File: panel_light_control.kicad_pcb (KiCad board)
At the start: 4 copper layers, 90 x 100 mm, 150 parts, among them J1 Conn_01x02, J11 RJ45_Shielded, J13 HR911105A, J2 RJ45_Shielded, J6 Conn_01x04, Q1 IRF540N, Q2 IRF540N, Q3 IRF540N, U1 L7805, U2 LM324, U3 STM32F207VGT6, U4 MCP2562-E-P, U5 LAN8720A, Y1 Crystal_GND24

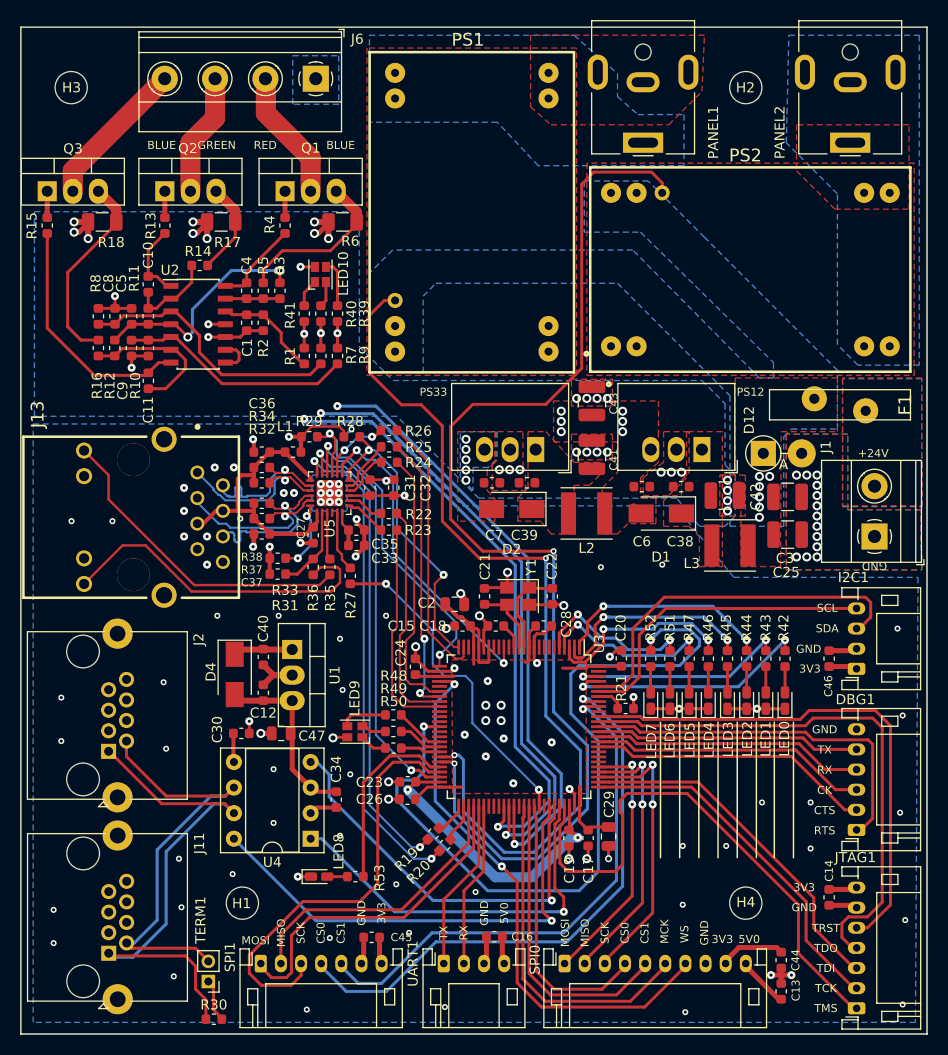
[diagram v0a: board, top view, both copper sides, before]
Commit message: Changes to 3.3V polygon shape to remove overlap with 24V, 12V input section. Some improvements and corrections to the silkscreen. 7805 location checked for 78B05 clearance - will work in case 5V >100 mA is needed :)
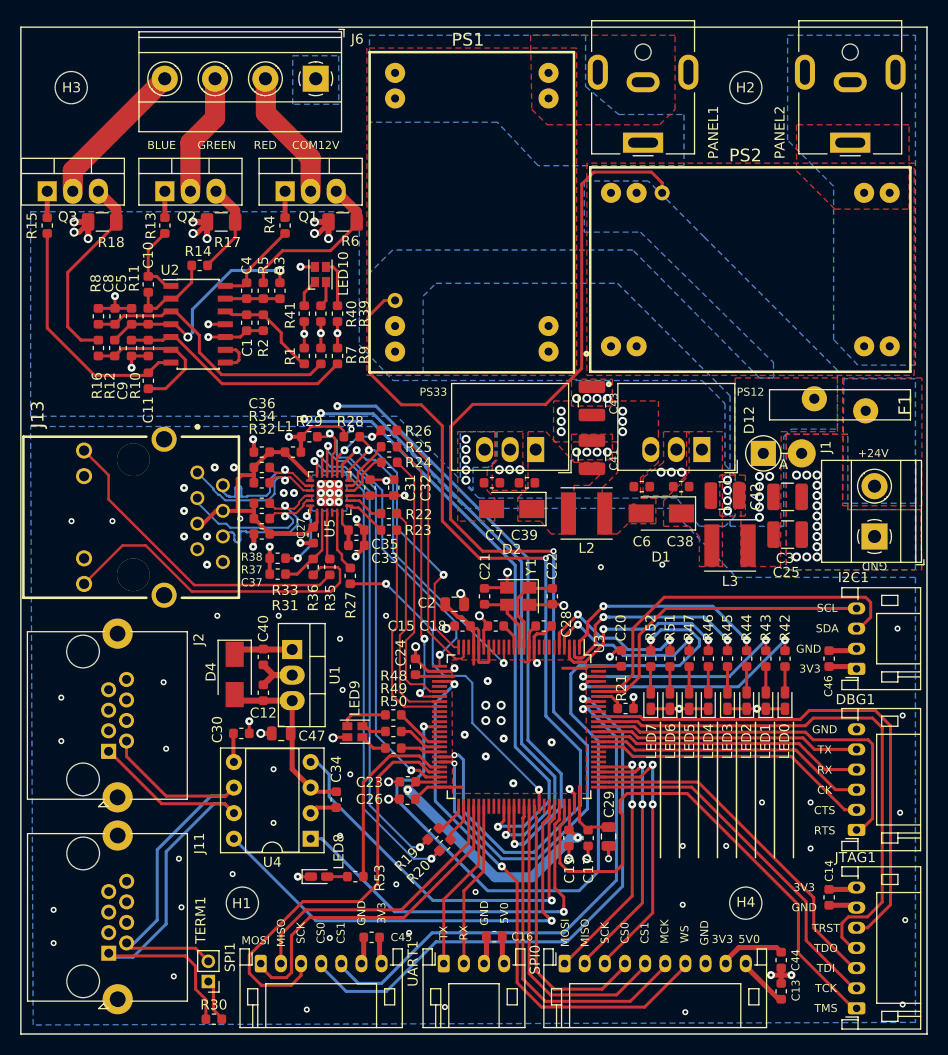
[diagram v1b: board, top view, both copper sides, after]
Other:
- board text added: "(+)"
- board text added: "+12VCOM"
- board text added: "1ACT"
- board text added: "2SPD"
- board text added: "CAN"
- board text added: "CANH"
- board text added: "CANL"
- board text added: "CAN_THRU"
- board text added: "COM12V"
- board text added: "DBG1"
- board text added: "I2C1"
- board text added: "JTAG1"
- board text added: "K_BLUE"
- board text added: "K_GREEN"
- board text added: "K_RED"
- board text added: "PANEL1"
- board text added: "PANEL2"
- board text added: "PWR IN"
- board text added: "RGB LED OUT"
- board text added: "RXN"
- board text added: "RXP"
- board text added: "SPI0/I2S"
- board text added: "SPI1"
- board text added: "TXN"
- board text added: "TXP"
- board text added: "UART1"
- board text removed: "+12V"
- board text removed: "BLUE-K"
- board text removed: "CAN1"
- board text removed: "CAN2"
- board text removed: "GREEN-K"
- board text removed: "RED-K"

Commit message: Added board art.
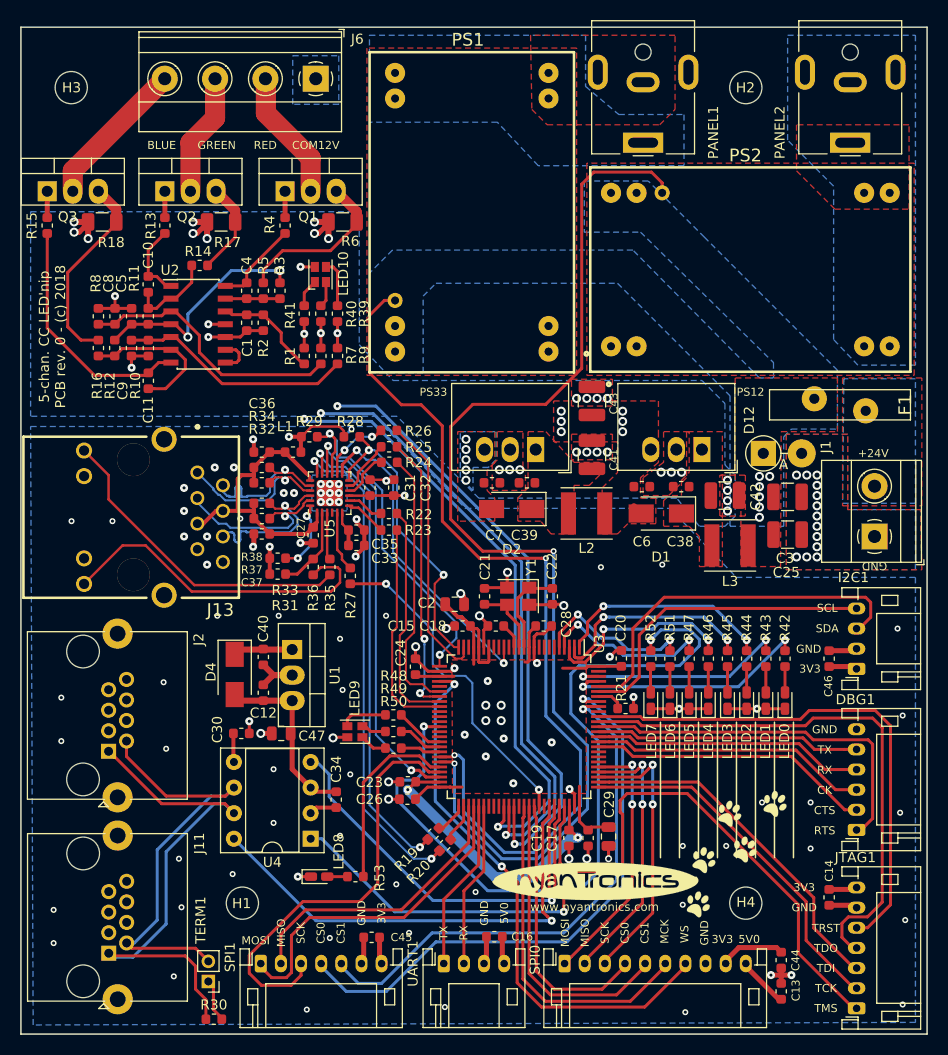
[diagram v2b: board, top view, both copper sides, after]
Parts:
- added G***: LOGO, oshw:oshw, B.Cu at (143.0, 66.1)
- added G***: LOGO, kicad_art:nyantronics_logo, F.Cu at (157.0, 134.7)
- added G***: LOGO, kicad_art:kitten_paw_prints, F.Cu at (171.1, 132.1)
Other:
- board text added: "5-chan. CC LED'nip PCB rev. 0 - (c) 2018"
- board text added: "www.nyantronics.com"

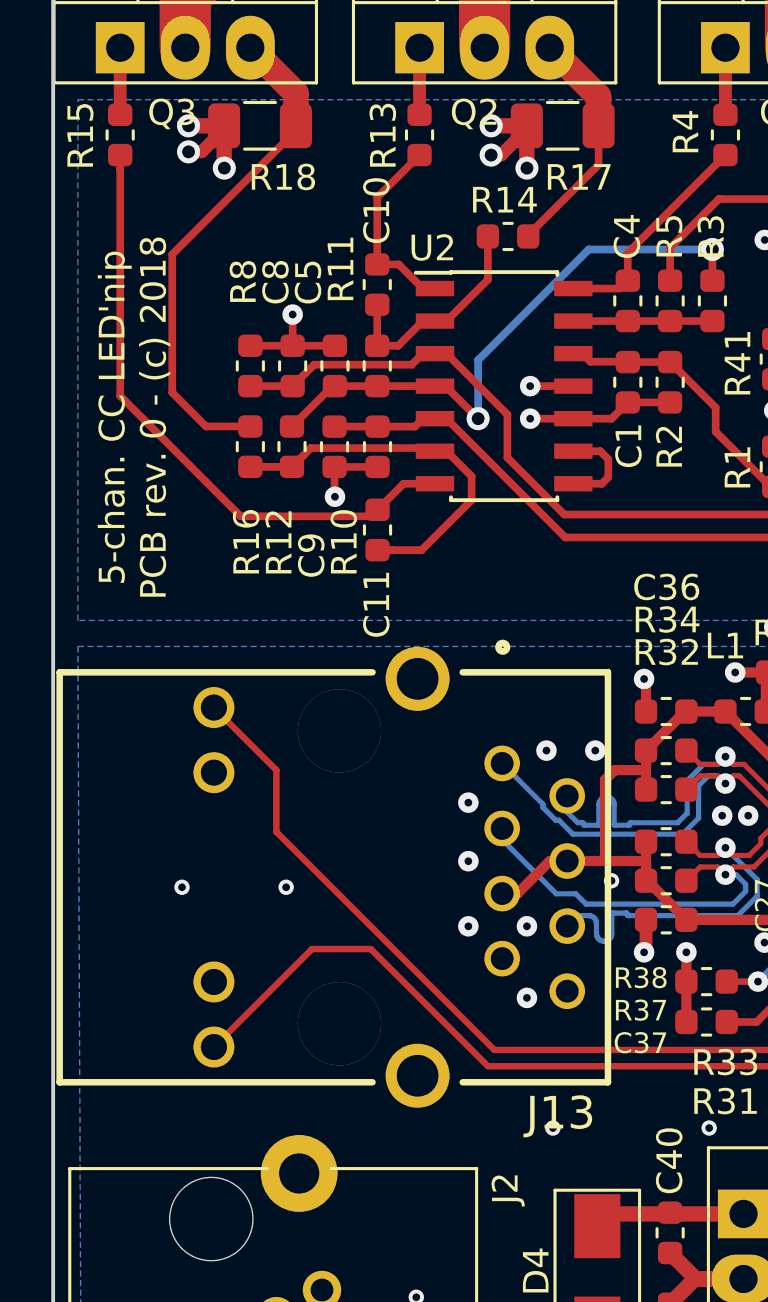
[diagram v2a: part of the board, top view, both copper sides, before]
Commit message: added BOM info, minor tweaks to artwork
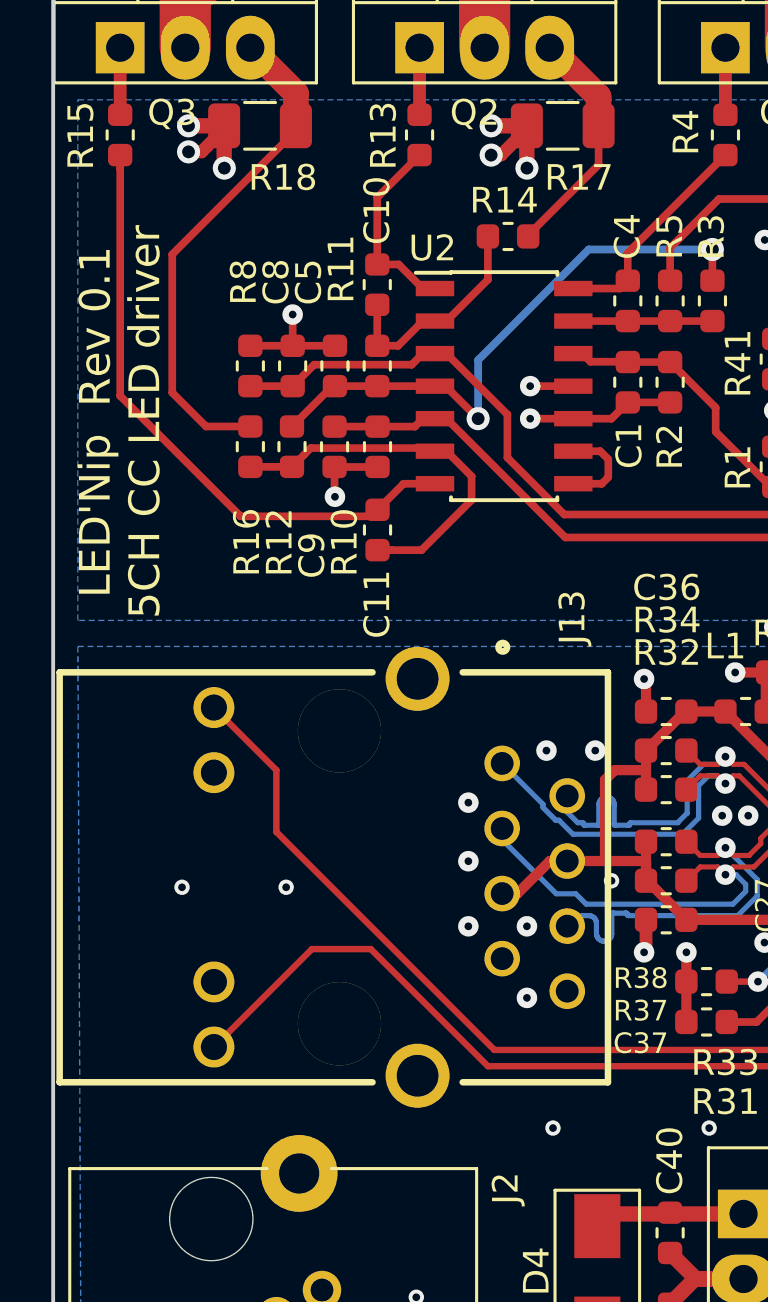
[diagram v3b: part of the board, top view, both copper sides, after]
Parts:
- R11, R12, R3: value 1M -> 4M7
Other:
- board text added: "LED'Nip Rev 0.1 5CH CC LED driver"
- board text removed: "5-chan. CC LED'nip PCB rev. 0 - (c) 2018"
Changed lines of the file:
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@@
-(kicad_pcb (version 20171130) (host pcbnew "(5.0.1)-rc2")
+(kicad_pcb (version 20171130) (host pcbnew "(6.0.0-rc1-dev-985-g576a0af29)")
   (general
     (thickness 1.6)
@@
     (zone_45_only no)
     (trace_min 0.2)
-    (segment_width 0.2)
-    (edge_width 0.15)
     (via_size 0.8)
     (via_drill 0.3)
@@
     (uvia_min_size 0.2)
     (uvia_min_drill 0.1)
+    (edge_width 0.15)
+    (segment_width 0.2)
     (pcb_text_width 0.3)
     (pcb_text_size 1.5 1.5)
@@
     (add_net TX_P)
   )
-  (module oshw:oshw (layer B.Cu)
+  (module oshw:oshw locked (layer B.Cu)
     (at 142.96644 66.09588 180)
     (fp_text reference G*** (at 0 0 180) (layer B.SilkS) hide
@@
       (effects (font (size 1 1) (thickness 0.15)))
     )
-    (fp_text value 1M (at 0 1.43 90) (layer F.Fab)
+    (fp_text value 4M7 (at 0 1.43 90) (layer F.Fab)
       (effects (font (size 1 1) (thickness 0.15)))
     )
@@
       (effects (font (size 1 1) (thickness 0.15)))
     )
-    (fp_text value 1M (at 0 1.43 90) (layer F.Fab)
+    (fp_text value 4M7 (at 0 1.43 90) (layer F.Fab)
       (effects (font (size 1 1) (thickness 0.15)))
     )
@@
     (descr HR911105A)
     (tags Connector)
-    (fp_text reference J13 (at -9.21258 5.588 180) (layer F.SilkS)
-      (effects (font (size 1.27 1.27) (thickness 0.254)))
+    (fp_text reference J13 (at 10.15238 6.0452 270) (layer F.SilkS)
+      (effects (font (size 1 1) (thickness 0.2)))
     )
     (fp_text value HR911105A (at 0.05588 -11.4173 90) (layer F.SilkS) hide
@@
       (effects (font (size 1 1) (thickness 0.15)))
     )
-    (fp_text value 1M (at 0 1.43 270) (layer F.Fab)
+    (fp_text value 4M7 (at 0 1.43 270) (layer F.Fab)
       (effects (font (size 1 1) (thickness 0.15)))
     )
@@
     )
   )
-  (module kicad_art:nyantronics_logo (layer F.Cu)
+  (module kicad_art:nyantronics_logo locked (layer F.Cu)
     (at 157.04312 134.747)
     (fp_text reference G*** (at 0 0) (layer F.SilkS) hide
@@
       (xy -0.939992 -1.772491) (xy -0.500661 -1.775565) (xy -0.047814 -1.77677) (xy 0.406741 -1.776106)) (layer F.SilkS) (width 0.01))
   )
-  (module kicad_art:kitten_paw_prints (layer F.Cu)
+  (module kicad_art:kitten_paw_prints locked (layer F.Cu)
     (at 171.0944 132.11556)
     (fp_text reference G*** (at 0 0) (layer F.SilkS) hide
@@
     (effects (font (size 0.84 0.84) (thickness 0.15)))
   )
-  (gr_text "5-chan. CC LED'nip\nPCB rev. 0 - (c) 2018 " (at 103.124 80.73136 90) (layer F.SilkS)
-    (effects (font (size 1 1) (thickness 0.2)))
+  (gr_text "LED'Nip  Rev 0.1\n5CH CC LED driver" (at 102.616 80.899 90) (layer F.SilkS)
+    (effects (font (size 1.2 1.2) (thickness 0.25)))
   )
   (gr_text RXN (at 122.301 100.6475) (layer B.SilkS)

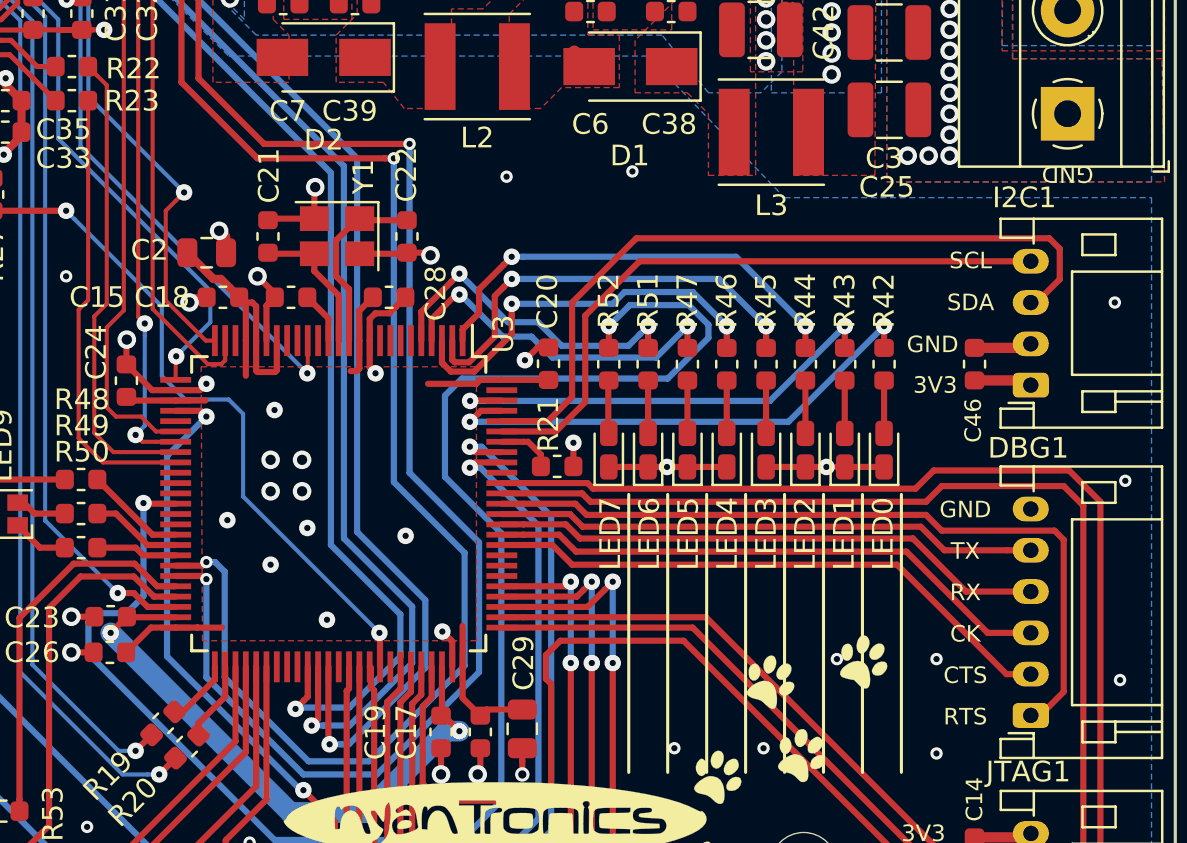
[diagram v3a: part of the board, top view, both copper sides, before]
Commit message: adds reset button, some xtal guarding. Schematic reviewed in this version, see https://hackmd.io/-iUjavK_Rz-11sfgLlTnuA# - xtal could be swapped for C_L 10 pF version to reduce susceptibility to environmental factors.
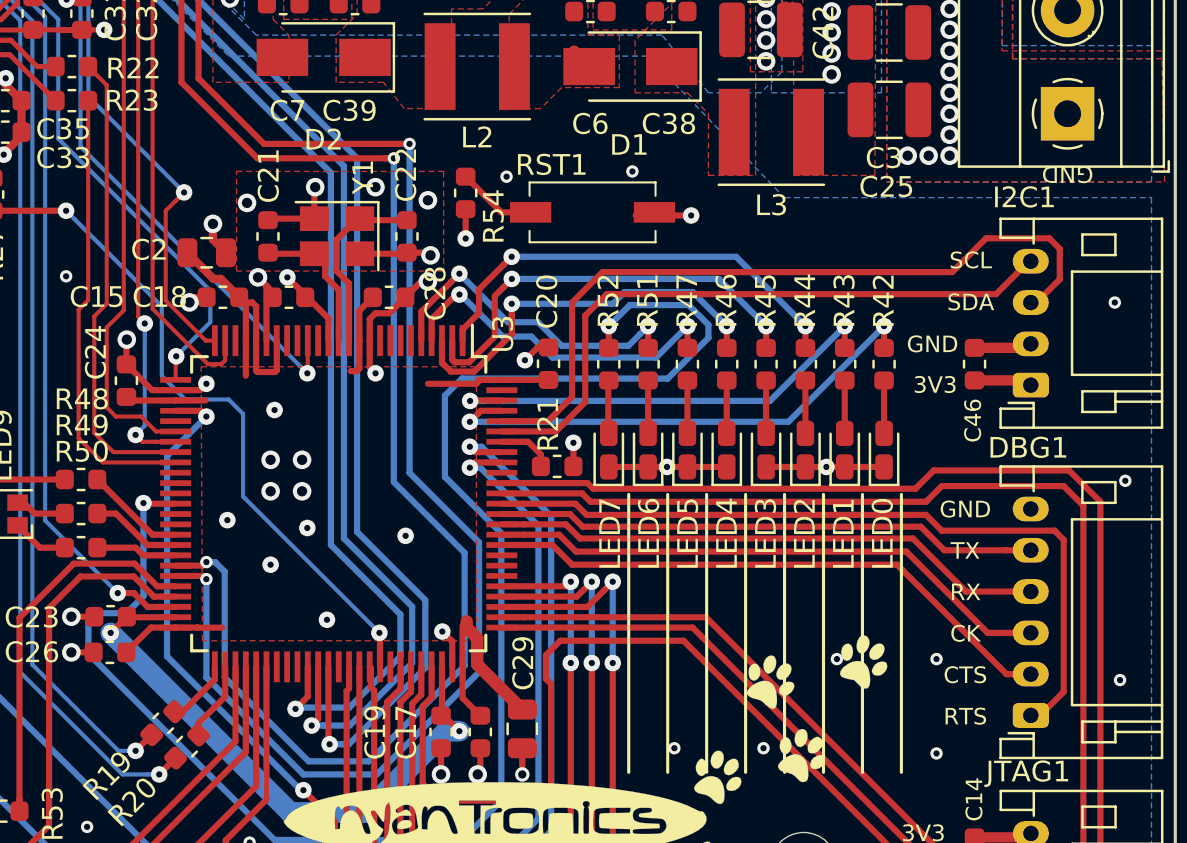
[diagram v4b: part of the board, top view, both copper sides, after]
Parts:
- added R54: 100R, Resistor_SMD:R_0603_1608Metric, F.Cu at (155.6, 104.4)
- added RST1: SKQYABE010, SamacSys_Parts:SKQYABE010, F.Cu at (161.8, 105.4)
- LED0, LED1, LED2, LED3, LED4, LED5, LED6, LED7: value LED_GN -> LED_AMB
- R42, R43, R44, R45, R46, R47, R51, R52, R53: value 120R -> 1k
- moved C18 0.10 mm to (147.1, 109.5)
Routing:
- net Net-(C18-Pad1): track 2.52 -> 15.4 mm, vias 0 -> 2
- net GND: track 120.1 -> 125.5 mm, vias 132 -> 137
- net Net-(R54-Pad2): track 0.00 -> 3.86 mm
- net +3.3V: track 73.4 -> 76.6 mm
